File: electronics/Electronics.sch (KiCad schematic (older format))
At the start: 21 parts

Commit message: Remapped MCU
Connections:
- net labels added: MCU-debug-LED_G1, MCU-debug-LED_G2, MCU-debug-LED_R1, MCU-debug-LED_R2
- net labels removed: MCU-debug-LED_1, MCU-debug-LED_2, MCU-debug-LED_3, MCU-debug-LED_4
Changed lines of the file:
@@
 Connection ~ 5350 3550
 Wire Wire Line
-	4300 2150 5100 2150
-Wire Wire Line
-	4300 2250 5100 2250
-Wire Wire Line
-	4300 2350 5100 2350
-Wire Wire Line
-	4300 2450 5100 2450
-Wire Wire Line
-	4300 2550 5100 2550
-Wire Wire Line
-	4300 2650 5100 2650
-Wire Wire Line
-	4300 2750 5100 2750
-Wire Wire Line
 	4300 3250 5100 3250
 Wire Wire Line
@@
 Wire Wire Line
 	700  3350 1700 3350
-Text Label 5100 2150 2    50   Italic 0
+Text Label 5100 3250 2    50   Italic 0
 MCU-MOT3en_2
-Text Label 5100 2250 2    50   Italic 0
+Text Label 5100 3350 2    50   Italic 0
 MCU-MOT1en_2
-Text Label 5100 2350 2    50   ~ 0
+Text Label 700  2750 0    50   ~ 0
 MCU-MOT3en_1
-Text Label 5100 2450 2    50   ~ 0
+Text Label 700  2850 0    50   ~ 0
 MCU-TRW_PWM
-Text Label 5100 2550 2    50   ~ 0
+Text Label 700  3150 0    50   ~ 0
 MCU-Hold-serv_PWM
-Text Label 5100 2650 2    50   ~ 0
+Text Label 700  3350 0    50   ~ 0
 MCU-mot_sleep
-Text Label 5100 2750 2    50   ~ 0
+Text Label 5100 2650 2    50   ~ 0
 MCU-mot_off
 Text HLabel 4600 2950 2    50   BiDi ~ 0
@@
 Wire Wire Line
 	4300 3150 4550 3150
-Text Label 5100 3250 2    50   ~ 0
+Text Label 700  3250 0    50   ~ 0
 MCU-Aim-serv_PWM
-Text HLabel 4350 3450 2    50   Input ~ 0
+Text HLabel 4350 2550 2    50   Input ~ 0
 MCU-mot1-enc_1
-Text HLabel 4350 3350 2    50   Input ~ 0
+Text HLabel 4350 2450 2    50   Input ~ 0
 MCU-mot1-enc_2
-Text HLabel 1450 3050 0    50   Input ~ 0
+Text HLabel 4350 2350 2    50   Input ~ 0
 MCU-mot2-enc_1
-Text HLabel 1450 2650 0    50   Input ~ 0
+Text HLabel 4350 2250 2    50   Input ~ 0
 MCU-mot2-enc_2
-Text HLabel 1450 3250 0    50   Input ~ 0
+Text HLabel 4350 2150 2    50   Input ~ 0
 MCU-mot3-enc_2
-Text HLabel 1450 3150 0    50   Input ~ 0
+Text HLabel 4350 2750 2    50   Input ~ 0
 MCU-mot3-enc_1
-Text Label 700  3350 0    50   ~ 0
+Text Label 5100 3450 2    50   ~ 0
 MCU-MOT1en_1
-Wire Wire Line
-	1450 3150 1700 3150
-Wire Wire Line
-	1450 3250 1700 3250
-Wire Wire Line
-	1450 3050 1700 3050
-Wire Wire Line
-	1450 2650 1700 2650
-Text Label 700  2750 0    50   ~ 0
+Text Label 700  2550 0    50   ~ 0
 MCU-MOT2en_1
-Text Label 700  2850 0    50   Italic 0
-MCU-MOT1en_2
-Wire Wire Line
-	4300 3350 4350 3350
-Wire Wire Line
-	4300 3450 4350 3450
+Text Label 700  2650 0    50   Italic 0
+MCU-MOT2en_2
 Text Notes 8050 2250 0    50   ~ 0
 Motor 1 and 2 PWM isolator
@@
 Text Notes 4100 7600 0    50   ~ 0
 Link to all connectors and voltage regulators
-Text Notes 2650 4100 0    50   ~ 0
+Text Notes 2750 4050 0    50   ~ 0
 STM32G4 MCU
 Text Notes 7350 7500 0    50   ~ 0
@@
 	3350 5250 3400 5250
 Text Label 700  2250 0    50   ~ 0
-MCU-debug-LED_3
+MCU-debug-LED_G1
 Text Label 700  2350 0    50   ~ 0
-MCU-debug-LED_4
-Text Label 700  2550 0    50   ~ 0
-MCU-debug-LED_1
+MCU-debug-LED_G2
 Text Label 700  2950 0    50   ~ 0
-MCU-debug-LED_2
+MCU-debug-LED_R1
+Text Label 700  3050 0    50   ~ 0
+MCU-debug-LED_R2
 Text Label 850  4700 0    50   ~ 0
-MCU-debug-LED_1
+MCU-debug-LED_R1
 Wire Wire Line
 	850  4700 1550 4700
 Text Label 850  5250 0    50   ~ 0
-MCU-debug-LED_2
+MCU-debug-LED_R2
 Wire Wire Line
 	850  5250 1550 5250
 Text Label 2350 5250 0    50   ~ 0
-MCU-debug-LED_4
+MCU-debug-LED_G2
 Wire Wire Line
 	2350 5250 3050 5250
 Text Label 2350 4700 0    50   ~ 0
-MCU-debug-LED_3
+MCU-debug-LED_G1
 Wire Wire Line
 	2350 4700 3050 4700
+Wire Wire Line
+	700  2650 1700 2650
+Wire Wire Line
+	700  3050 1700 3050
+Wire Wire Line
+	700  3150 1700 3150
+Wire Wire Line
+	700  3250 1700 3250
+Wire Wire Line
+	4300 3450 5100 3450
+Wire Wire Line
+	4300 3350 5100 3350
+Wire Wire Line
+	4300 2650 5100 2650
+Wire Wire Line
+	4300 2750 4350 2750
+Wire Wire Line
+	4300 2550 4350 2550
+Wire Wire Line
+	4300 2450 4350 2450
+Wire Wire Line
+	4300 2350 4350 2350
+Wire Wire Line
+	4300 2250 4350 2250
+Wire Wire Line
+	4300 2150 4350 2150
 $EndSCHEMATC

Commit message: Updated rev numbers
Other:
- note added: "1.1"
- note added: "24/10/2021"
- note removed: "1.0"
- note removed: "21/10/2021"
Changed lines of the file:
@@
 CPU and isolators
 Text Notes 8100 7650 0    50   ~ 0
-21/10/2021
+24/10/2021
 Text Notes 10550 7650 0    50   ~ 0
-1.0
+1.1
 $Bitmap
 Pos 7450 6850

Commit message: Attached footprints to components
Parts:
- C1, C3, C4, C5, C6, C7, C8, C9: renamed from C?; footprint (none) -> Capacitor_SMD:C_0603_1608Metric_Pad1.08x0.95mm_HandSolder
- C2: renamed from C?; footprint (none) -> Capacitor_THT:CP_Radial_D5.0mm_P2.00mm
- D1, D2, D3, D4: renamed from D?; footprint (none) -> LED_SMD:LED_0603_1608Metric_Pad1.05x0.95mm_HandSolder
- R1, R2, R3, R4: renamed from R?; footprint (none) -> Resistor_SMD:R_0603_1608Metric_Pad0.98x0.95mm_HandSolder
- U1: renamed from U?; footprint LQFP32_7X7_STM -> Electronics:STM32G441KBT3
- U2, U3, U4: renamed from U?; footprint 21-0041_S16+1_MXM -> Electronics:MAX14930DASE&plus_

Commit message: Spurdo commit
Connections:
- net labels removed: MOT1en_1, MOT1en_2, MOT2en_1, MOT2en_2, MOT3en_1, MOT3en_2, MOT_off, MOT_sleep
- wire segments 85 -> 123
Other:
- note added: "31/10/2021"
- note removed: "24/10/2021"
- moved on the sheet: C4, C5, C6, C7, C8, C9

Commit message: Relocated libs, renamed MCU
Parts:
- U1: symbol 2021-09-13_09-53-18:STM32G441KBT3 -> STM32G441KB:STM32G441KBT3
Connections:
- wire segments 123 -> 122
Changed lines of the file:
@@
 Wire Wire Line
 	700  2250 1700 2250
-Connection ~ 1700 2050
-Wire Wire Line
-	1700 2150 1700 2050
-Connection ~ 1700 3550
 Wire Wire Line
 	1700 3450 1700 3550
 $Comp
-L 2021-09-13_09-53-18:STM32G441KBT3 U1
+L STM32G441KB:STM32G441KBT3 U1
 U 1 1 617240B4
 P 1700 2050
@@
 $EndComp
 Connection ~ 2000 1550
-Wire Wire Line
-	1700 2050 1700 1550
 Wire Wire Line
 	1700 1250 1700 1550
@@
 Wire Wire Line
 	3350 6300 3950 6300
+Wire Wire Line
+	1700 1550 1700 2150
 $EndSCHEMATC

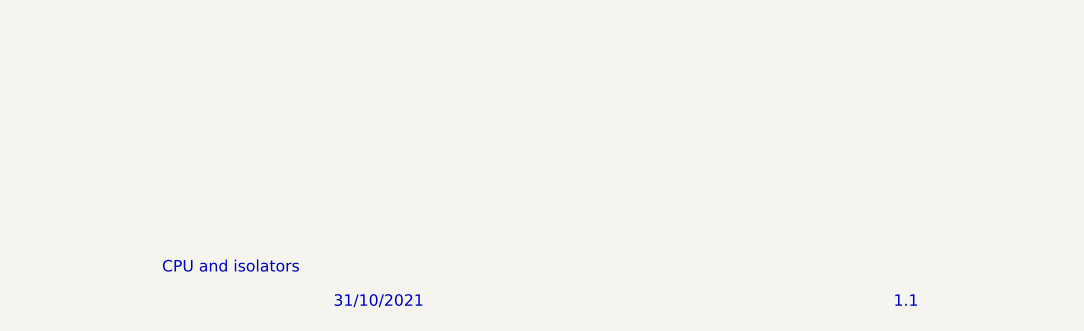
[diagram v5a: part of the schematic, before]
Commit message: Figured out how to automatically change date and revision
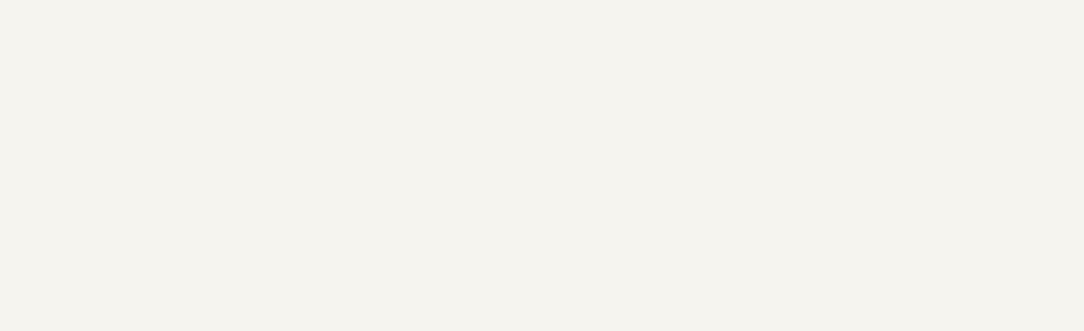
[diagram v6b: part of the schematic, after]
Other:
- note removed: "1.1"
- note removed: "31/10/2021"
- note removed: "CPU and isolators"
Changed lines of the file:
@@
 encoding utf-8
 Sheet 1 3
-Title ""
-Date ""
-Rev ""
+Title "CPU and isolators"
+Date "2021-11-01"
+Rev "1.2"
 Comp ""
 Comment1 ""
@@
 Comment4 ""
 $EndDescr
-Text Notes 7350 7500 0    50   ~ 0
-CPU and isolators
-Text Notes 8100 7650 0    50   ~ 0
-31/10/2021
-Text Notes 10550 7650 0    50   ~ 0
-1.1
 $Bitmap
 Pos 7450 6850

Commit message: Relocated items
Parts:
- removed C2: 4.7uF, Capacitor_THT:CP_Radial_D5.0mm_P2.00mm, symbol Device:CP
- added C2, C31: 4.7uF, Capacitor_SMD:C_1206_3216Metric_Pad1.33x1.80mm_HandSolder, symbol Device:C
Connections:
- wire segments 122 -> 124
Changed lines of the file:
@@
 	2000 1550 2150 1550
-$Comp
-L Device:CP C?
-U 1 1 617240AB
-P 1850 1550
-AR Path="/613FDA12/617240AB" Ref="C?"  Part="1"
-AR Path="/617240AB" Ref="C2"  Part="1"
-F 0 "C2" V 2105 1550 50  0000 C CNN
-F 1 "4.7uF" V 2014 1550 50  0000 C CNN
-F 2 "Capacitor_THT:CP_Radial_D5.0mm_P2.00mm" H 1888 1400 50  0001 C CNN
-F 3 "~" H 1850 1550 50  0001 C CNN
-	1    1850 1550
-	0    1    1    0
-$EndComp
-Wire Wire Line
-	2000 1250 2000 1550
 $Comp
 L power:GND #PWR?
@@
 	1    0    0    -1
 $EndComp
-Connection ~ 2000 1550
-Wire Wire Line
-	1700 1250 1700 1550
-Connection ~ 1700 1550
 Connection ~ 1700 1250
 Wire Wire Line
@@
 Connection ~ 5350 3550
 Wire Wire Line
-	4300 3550 5350 3550
+	4300 3550 4950 3550
 $Comp
 L Device:C C?
@@
 	3350 6300 3950 6300
 Wire Wire Line
-	1700 1550 1700 2150
+	2000 1250 2000 1550
+$Comp
+L Device:C C?
+U 1 1 61834ECC
+P 1850 1550
+AR Path="/613FDA12/61834ECC" Ref="C?"  Part="1"
+AR Path="/61834ECC" Ref="C2"  Part="1"
+F 0 "C2" V 1700 1550 50  0000 C CNN
+F 1 "4.7uF" V 1600 1550 50  0000 C CNN
+F 2 "Capacitor_SMD:C_1206_3216Metric_Pad1.33x1.80mm_HandSolder" H 1888 1400 50  0001 C CNN
+F 3 "~" H 1850 1550 50  0001 C CNN
+	1    1850 1550
+	0    -1   -1   0
+$EndComp
+Wire Wire Line
+	1700 1250 1700 1550
+Connection ~ 1700 1550
+Wire Wire Line
+	1700 1550 1700 2050
+Connection ~ 2000 1550
+Connection ~ 1700 2050
+Wire Wire Line
+	1700 2050 1700 2150
+$Comp
+L Device:C C?
+U 1 1 618E44E9
+P 4950 3700
+AR Path="/613FDA12/618E44E9" Ref="C?"  Part="1"
+AR Path="/618E44E9" Ref="C31"  Part="1"
+F 0 "C31" H 5064 3654 50  0000 L CNN
+F 1 "4.7uF" H 5064 3745 50  0000 L CNN
+F 2 "Capacitor_SMD:C_1206_3216Metric_Pad1.33x1.80mm_HandSolder" H 4988 3550 50  0001 C CNN
+F 3 "~" H 4950 3700 50  0001 C CNN
+	1    4950 3700
+	-1   0    0    1
+$EndComp
+$Comp
+L power:GND #PWR?
+U 1 1 618EA48D
+P 4950 3850
+AR Path="/613FDA12/618EA48D" Ref="#PWR?"  Part="1"
+AR Path="/618EA48D" Ref="#PWR0188"  Part="1"
+F 0 "#PWR0188" H 4950 3600 50  0001 C CNN
+F 1 "GND" H 4955 3677 50  0000 C CNN
+F 2 "" H 4950 3850 50  0001 C CNN
+F 3 "" H 4950 3850 50  0001 C CNN
+	1    4950 3850
+	1    0    0    -1
+$EndComp
+Connection ~ 4950 3550
+Wire Wire Line
+	4950 3550 5350 3550
 $EndSCHEMATC

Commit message: Moved usb
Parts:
- added H1, H2, H3, H4: MountingHole, MountingHole:MountingHole_3.2mm_M3, symbol Mechanical:MountingHole
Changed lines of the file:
@@
 Wire Wire Line
 	4950 3550 5350 3550
+$Comp
+L Mechanical:MountingHole H1
+U 1 1 61816050
+P 1000 6300
+F 0 "H1" H 1100 6346 50  0000 L CNN
+F 1 "MountingHole" H 1100 6255 50  0000 L CNN
+F 2 "MountingHole:MountingHole_3.2mm_M3" H 1000 6300 50  0001 C CNN
+F 3 "~" H 1000 6300 50  0001 C CNN
+	1    1000 6300
+	1    0    0    -1
+$EndComp
+$Comp
+L Mechanical:MountingHole H2
+U 1 1 61816B61
+P 1000 6550
+F 0 "H2" H 1100 6596 50  0000 L CNN
+F 1 "MountingHole" H 1100 6505 50  0000 L CNN
+F 2 "MountingHole:MountingHole_3.2mm_M3" H 1000 6550 50  0001 C CNN
+F 3 "~" H 1000 6550 50  0001 C CNN
+	1    1000 6550
+	1    0    0    -1
+$EndComp
+$Comp
+L Mechanical:MountingHole H3
+U 1 1 6181C2C0
+P 1000 6800
+F 0 "H3" H 1100 6846 50  0000 L CNN
+F 1 "MountingHole" H 1100 6755 50  0000 L CNN
+F 2 "MountingHole:MountingHole_3.2mm_M3" H 1000 6800 50  0001 C CNN
+F 3 "~" H 1000 6800 50  0001 C CNN
+	1    1000 6800
+	1    0    0    -1
+$EndComp
+$Comp
+L Mechanical:MountingHole H4
+U 1 1 61843A2A
+P 1000 7050
+F 0 "H4" H 1100 7096 50  0000 L CNN
+F 1 "MountingHole" H 1100 7005 50  0000 L CNN
+F 2 "MountingHole:MountingHole_3.2mm_M3" H 1000 7050 50  0001 C CNN
+F 3 "~" H 1000 7050 50  0001 C CNN
+	1    1000 7050
+	1    0    0    -1
+$EndComp
 $EndSCHEMATC
